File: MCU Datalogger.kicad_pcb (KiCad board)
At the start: 2 copper layers, 29 parts, among them J1 Conn_01x09_Male, J2 Conn_01x04_Male, J3 Conn_02x03_Odd_Even, J4 Conn_01x04_Male, U1 24LC1025, U2 DS1337S+, U3 24LC1025, U4 ATMEGA328P-AU, Y1 32.768 KHz, Y2 16MHz

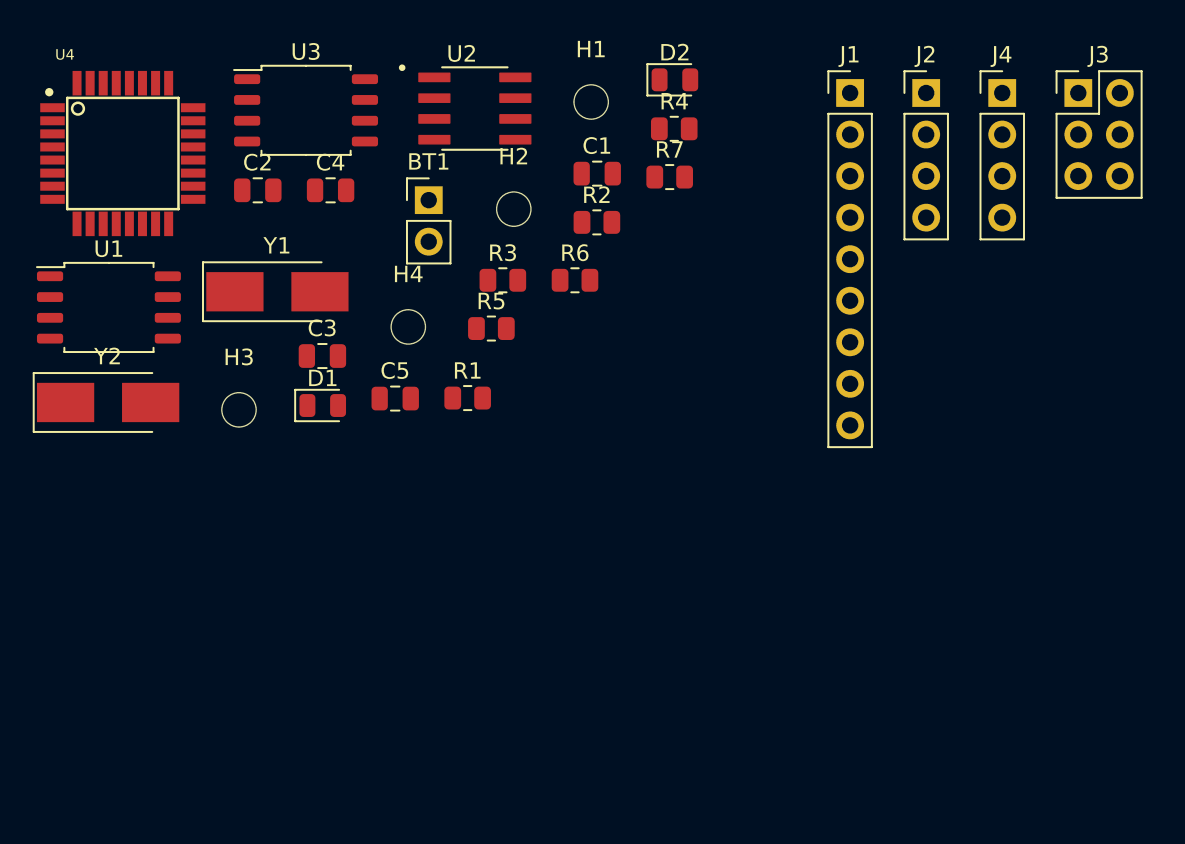
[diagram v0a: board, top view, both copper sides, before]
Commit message: Did the initial add and positioning of footprints on the PCB
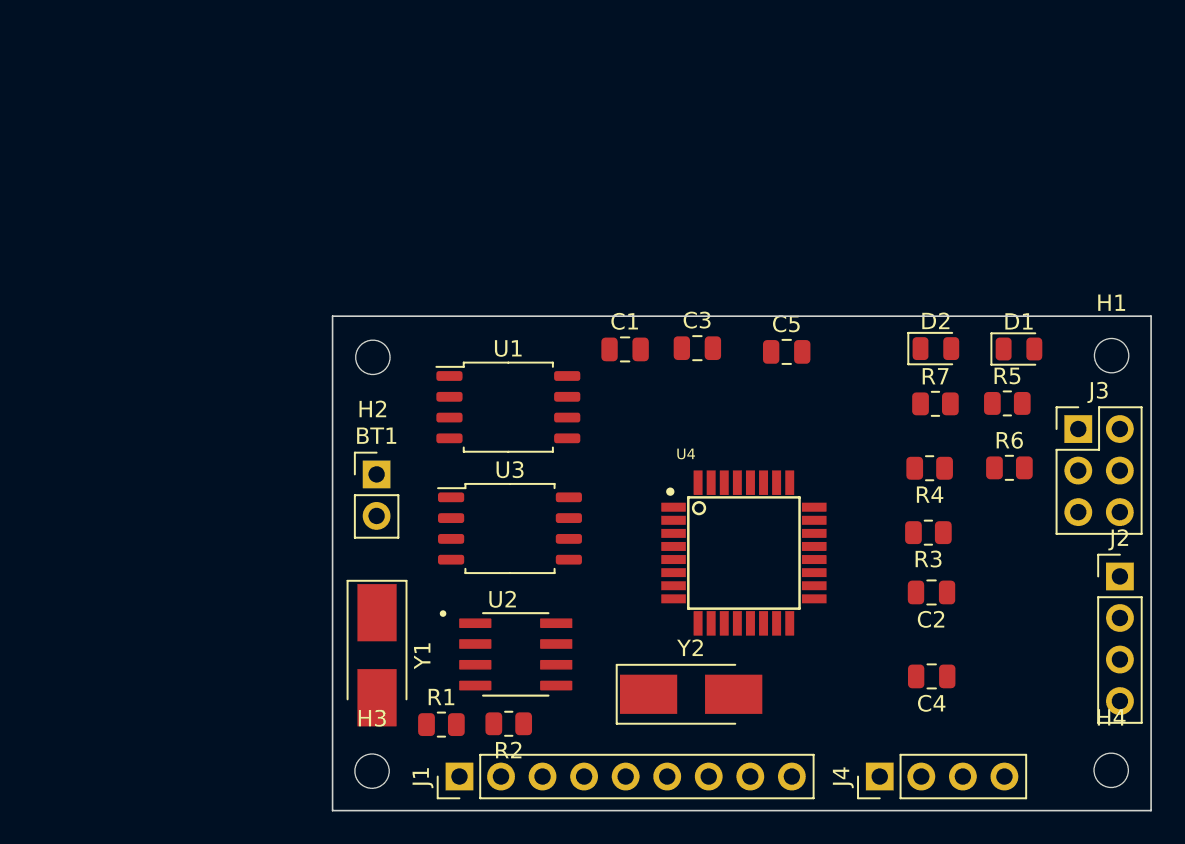
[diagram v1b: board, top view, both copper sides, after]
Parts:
- moved H4 50.8 mm to (148.3, 111.8)
- moved J1 48.1 mm to (108.5, 112.2), turned to 90 degrees
- moved C2 48.0 mm to (137.3, 101.0), turned to 180 degrees
- moved C4 47.3 mm to (137.3, 106.1), turned to 180 degrees
- moved U4 45.1 mm to (125.9, 98.6)
- moved D1 42.7 mm to (142.7, 86.1)
- moved J4 42.5 mm to (134.2, 112.2), turned to 90 degrees
- moved Y2 39.9 mm to (122.6, 107.2)
- moved H1 35.4 mm to (148.3, 86.5)
- moved U2 33.5 mm to (111.9, 104.7)
- moved R5 31.9 mm to (142.0, 89.4)
- moved J2 31.8 mm to (148.8, 100.0)
- moved R2 31.1 mm to (111.5, 109.0), turned to 180 degrees
- moved R3 30.2 mm to (137.1, 97.3), turned to 180 degrees
- moved R6 28.9 mm to (142.1, 93.3)
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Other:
- board outline added: 50 x 30.2 mm

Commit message: beginning routing
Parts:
- moved U1 2.66 mm to (110.6, 87.1)
- moved C3 2.01 mm to (121.2, 85.2)
- moved C1 1.46 mm to (117.4, 85.2)
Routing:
- net GND: track 0.00 -> 6.58 mm
- net /Vcc: track 0.00 -> 2.32 mm
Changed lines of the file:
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@@
   )
   (footprint "Capacitor_SMD:C_0805_2012Metric" (layer "F.Cu")
-    (at 123.0122 86.0298)
+    (at 121.1834 85.1916)
     (descr "Capacitor SMD 0805 (2012 Metric), square (rectangular) end terminal, IPC_7351 nominal, (Body size source: IPC-SM-782 page 76, https://www.pcb-3d.com/wordpress/wp-content/uploads/ipc-sm-782a_amendment_1_and_2.pdf, https://docs.google.com/spreadsheets/d/1BsfQQcO9C6DZCsRaXUlFlo91Tg2WpOkGARC1WS5S8t0/edit?usp=sharing), generated with kicad-footprint-generator")
     (tags "capacitor")
@@
   )
   (footprint "Capacitor_SMD:C_0805_2012Metric" (layer "F.Cu")
-    (at 118.5926 86.106)
+    (at 117.4496 85.1916)
     (descr "Capacitor SMD 0805 (2012 Metric), square (rectangular) end terminal, IPC_7351 nominal, (Body size source: IPC-SM-782 page 76, https://www.pcb-3d.com/wordpress/wp-content/uploads/ipc-sm-782a_amendment_1_and_2.pdf, https://docs.google.com/spreadsheets/d/1BsfQQcO9C6DZCsRaXUlFlo91Tg2WpOkGARC1WS5S8t0/edit?usp=sharing), generated with kicad-footprint-generator")
     (tags "capacitor")
@@
   )
   (footprint "Package_SO:SOIC-8_5.23x5.23mm_P1.27mm" (layer "F.Cu")
-    (at 111.4552 89.6366)
+    (at 110.5916 87.122)
     (descr "SOIC, 8 Pin (http://www.winbond.com/resource-files/w25q32jv%20revg%2003272018%20plus.pdf#page=68), generated with kicad-footprint-generator ipc_gullwing_generator.py")
     (tags "SOIC SO")
@@
   )
   (gr_rect (start 100.711 84.074) (end 150.749 114.3) (layer "Edge.Cuts") (width 0.1) (fill none))
+  (segment (start 120.2334 85.1916) (end 118.3996 85.1916) (width 0.35) (layer "F.Cu") (net 2))
+  (segment (start 117.1042 86.487) (end 118.3996 85.1916) (width 0.35) (layer "F.Cu") (net 2))
+  (segment (start 114.1916 86.487) (end 117.1042 86.487) (width 0.35) (layer "F.Cu") (net 2))
+  (segment (start 116.4742 85.217) (end 116.4996 85.1916) (width 0.35) (layer "F.Cu") (net 3))
+  (segment (start 114.1916 85.217) (end 116.4742 85.217) (width 0.35) (layer "F.Cu") (net 3))
 )

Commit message: re-import the footprints into the PCB editor.
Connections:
- J2 pad 4: /SCK -> /SCL
- R3 pad 2: /SCK -> /SCL
- U1 pad 6: /SCK -> /SCL
- U2 pad 6: /SCK -> /SCL
- U3 pad 6: /SCK -> /SCL
- U4 pad 28: /SCK -> /SCL

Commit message: More routing. Right before I decided to go back to the screwed up schematic and exactly match his errors
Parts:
- moved C2 19.3 mm to (118.0, 100.2), turned to 0 degrees
- moved R3 15.2 mm to (126.0, 86.9), turned to -90 degrees
- moved R4 11.3 mm to (128.0, 86.9), turned to -90 degrees
- moved U3 10.0 mm to (110.6, 87.1)
- moved C4 9.61 mm to (133.9, 97.1), turned to -90 degrees
- moved J4 7.60 mm to (141.8, 112.4), turned to -90 degrees
- moved U1 7.60 mm to (111.2, 94.7)
- moved R5 5.68 mm to (138.0, 85.3)
- moved C5 4.87 mm to (133.2, 85.3)
- moved D2 4.67 mm to (133.2, 87.7), turned to 180 degrees
- moved D1 3.55 mm to (141.4, 89.4)
- moved U2 2.35 mm to (110.5, 102.8)
- moved Y2 2.31 mm to (120.3, 107.5), turned to 180 degrees
- moved U4 1.96 mm to (127.1, 97.1)
- moved R6 1.91 mm to (141.4, 95.1)
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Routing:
- net /Vcc: track 2.32 -> 150.0 mm, vias 0 -> 6
- net /SCL: track 0.00 -> 70.2 mm, vias 0 -> 1
- net /SDA: track 0.00 -> 68.2 mm, vias 0 -> 4
- net GND: track 6.58 -> 62.9 mm, vias 0 -> 6
- net Net-(BT1-Pad1): track 0.00 -> 43.4 mm, vias 0 -> 3
- net /D2: track 0.00 -> 29.8 mm
- net /TX: track 0.00 -> 29.4 mm, vias 0 -> 1
- net /RX: track 0.00 -> 29.0 mm, vias 0 -> 1
- net /RESET: track 0.00 -> 27.9 mm, vias 0 -> 1
- net /MOSI: track 0.00 -> 25.2 mm
- net /D3: track 0.00 -> 25.2 mm
- net /SCK: track 0.00 -> 24.5 mm, vias 0 -> 2
- net /D4: track 0.00 -> 23.2 mm
- net /D5: track 0.00 -> 18.1 mm
- net /D6: track 0.00 -> 16.0 mm
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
